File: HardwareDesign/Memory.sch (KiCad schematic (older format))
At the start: 4 parts, among them U200 28C256, U201 HM62256BLP-7SL

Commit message: more work on preparing for PCB design
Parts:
- added J201: Conn_02x40_Counter_Clockwise, symbol Connector_Generic:Conn_02x40_Counter_Clockwise
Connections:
- net labels added: E, PC0, PC1, PC2, PC3, PC4, PC5, PC6, PC7, RST, R~W, TIRQ, ~IODEV0, ~IODEV1, ~IODEV10, ~IODEV11, ~IODEV12, ~IODEV13, ~IODEV14, ~IODEV15, ~IODEV2, ~IODEV3, ~IODEV4, ~IODEV5, ~IODEV6, ~IODEV7, ~IODEV8, ~IODEV9, ~IRQ, ~RST~
- wire segments 95 -> 179
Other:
- note added: "back row"
- note added: "backplane connector"
- note added: "front row"
- moved on the sheet: C200, C201, U201

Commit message: more cleanups in preparation for PCB layout
Renamed nets to distinguish unbuffered vs. buffered signals.

Fixed one error in interrupt controller (D0 was tied
to ground.)

Not entirely done yet.
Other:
- note added: "back row (backplane)\nbottom row (board)"
- note added: "front row (backplane)\ntop row (board)"
- note removed: "back row"
- note removed: "front row"
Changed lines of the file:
@@
 Wire Wire Line
 	9050 5600 9600 5600
-Text Notes 8000 1450 0    50   ~ 0
-back row
-Text Notes 9300 1450 0    50   ~ 0
-front row
 Text Label 9400 1800 0    50   ~ 0
 D0
@@
 Wire Wire Line
 	7750 5950 7750 5850
+$Comp
+L power:VCC #PWR?
+U 1 1 60AC3A0A
+P 7750 5850
+F 0 "#PWR?" H 7750 5700 50  0001 C CNN
+F 1 "VCC" H 7767 6023 50  0000 C CNN
+F 2 "" H 7750 5850 50  0001 C CNN
+F 3 "" H 7750 5850 50  0001 C CNN
+	1    7750 5850
+	1    0    0    -1
+$EndComp
+Text Notes 7850 1500 0    50   ~ 0
+back row (backplane)\nbottom row (board)
+Text Notes 9000 1500 0    50   ~ 0
+front row (backplane)\ntop row (board)
 Wire Bus Line
 	3400 2950 6450 2950
@@
 Wire Bus Line
 	1500 1300 1500 3050
-$Comp
-L power:VCC #PWR?
-U 1 1 60AC3A0A
-P 7750 5850
-F 0 "#PWR?" H 7750 5700 50  0001 C CNN
-F 1 "VCC" H 7767 6023 50  0000 C CNN
-F 2 "" H 7750 5850 50  0001 C CNN
-F 3 "" H 7750 5850 50  0001 C CNN
-	1    7750 5850
-	1    0    0    -1
-$EndComp
 $EndSCHEMATC

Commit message: more preparations for PCB layout
More nets connected to appropriate backplane connector pin.
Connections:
- net labels added: ~IOR1~, ~IOR2~, ~IOR3~, ~IOR4~, ~IOR5~, ~IOR6~, ~IOR7~
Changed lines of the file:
@@
 Text Notes 9000 1500 0    50   ~ 0
 front row (backplane)\ntop row (board)
+Text Label 8100 3300 0    50   ~ 0
+~IOR1~
+Text Label 8100 3400 0    50   ~ 0
+~IOR2~
+Text Label 8100 3500 0    50   ~ 0
+~IOR3~
+Text Label 8100 3600 0    50   ~ 0
+~IOR4~
+Text Label 8100 3700 0    50   ~ 0
+~IOR5~
+Text Label 8100 3800 0    50   ~ 0
+~IOR6~
+Text Label 8100 3900 0    50   ~ 0
+~IOR7~
 Wire Bus Line
 	3400 2950 6450 2950

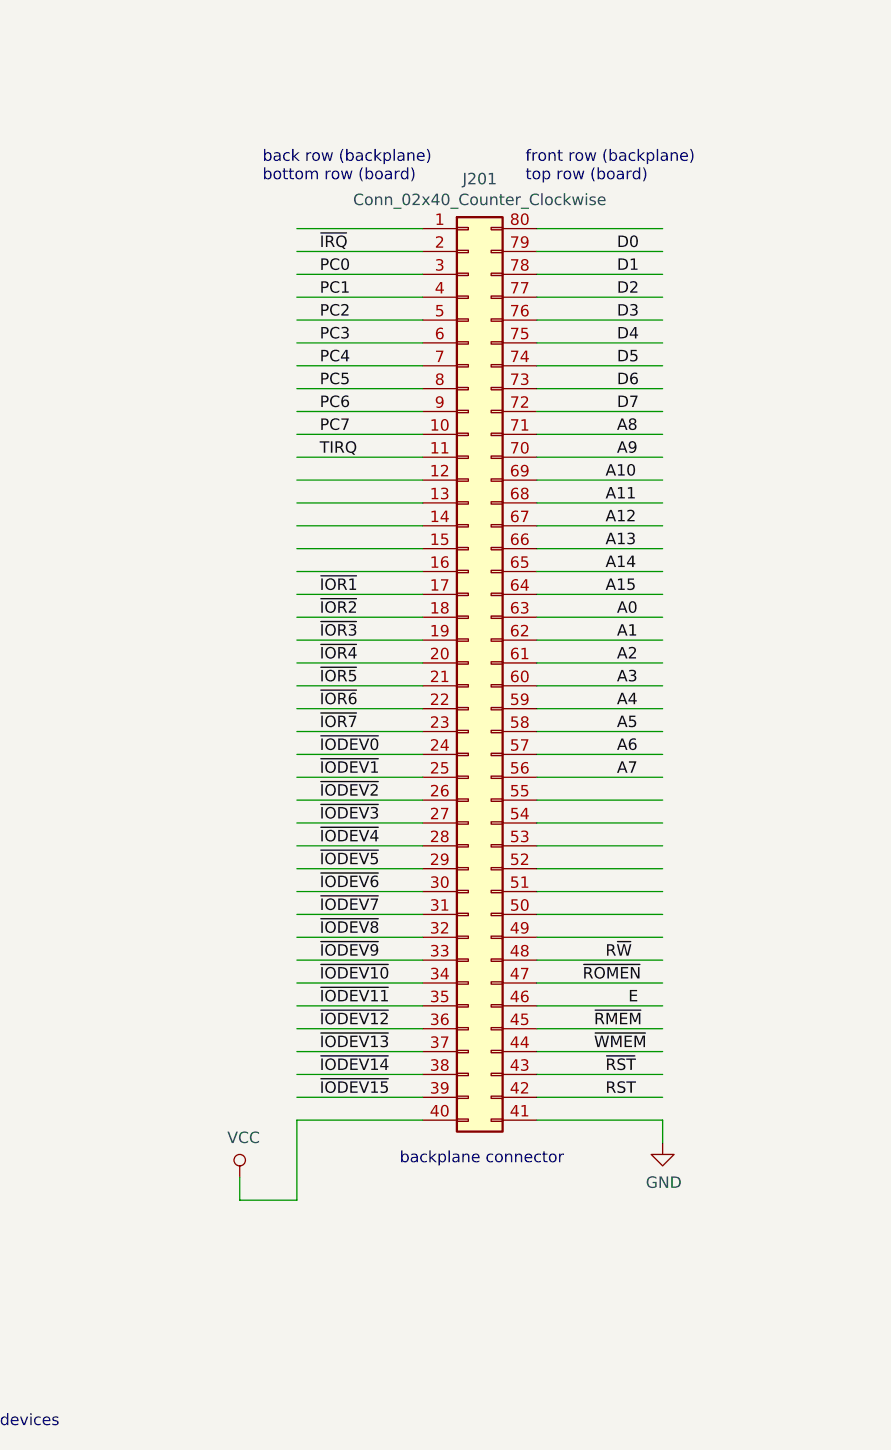
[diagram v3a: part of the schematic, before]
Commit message: more preparations for PCB layout
Make sure all nets connected to backplane connector pins are
labeled correctly.

Add bulk decoupling caps for each backplane connector.

Make keyboard interrupt be -IRQ5 rather than -IRQ7.
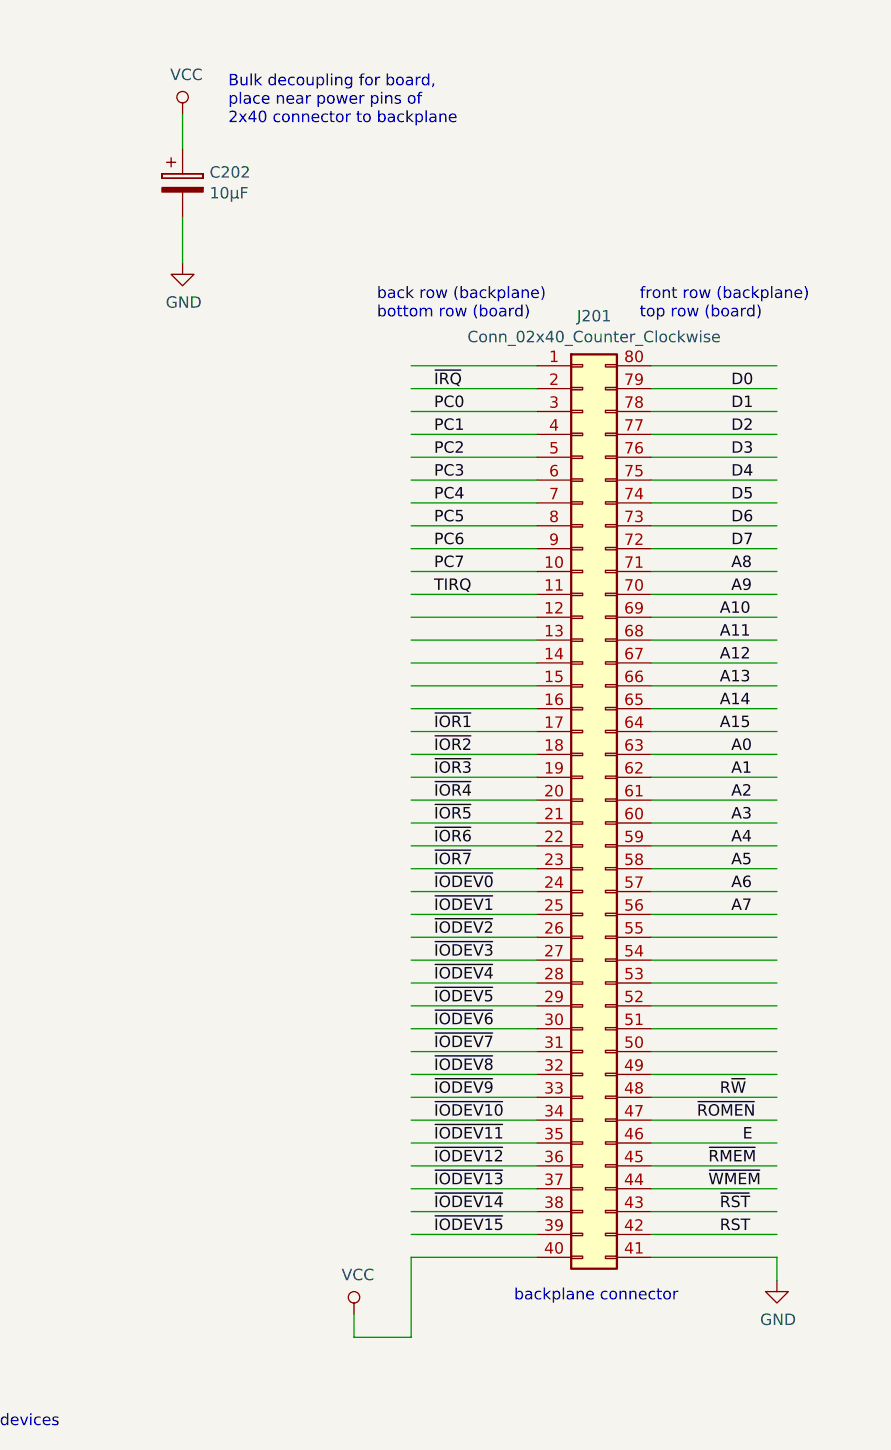
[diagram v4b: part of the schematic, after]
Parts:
- added C202: 10μF, symbol device:CP
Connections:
- wire segments 179 -> 181
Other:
- note added: "Bulk decoupling for board,\nplace near power pins of\n2x40 connector to backplane"
- moved on the sheet: J201

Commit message: a few more consistency tweaks before PCB layout
Routed second timer/counter output to backplane connector,
just in case we want to use it for something eventually
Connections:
- net labels added: TCOUNT2
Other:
- note added: "TCOUNT2 shown here\nto allow second\ntimer/counter output\nto connect to backplane"
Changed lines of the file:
@@
 U 1 1 60CC0A73
 P 7500 1200
+AR Path="/5CFA6AAA/60CC0A73" Ref="#PWR?"  Part="1"
+AR Path="/5D49B078/60CC0A73" Ref="#PWR?"  Part="1"
 F 0 "#PWR?" H 7500 1050 50  0001 C CNN
 F 1 "VCC" H 7517 1373 50  0000 C CNN
@@
 U 1 1 60CC0A7A
 P 7500 1850
+AR Path="/5CFA6AAA/60CC0A7A" Ref="#PWR?"  Part="1"
+AR Path="/5D49B078/60CC0A7A" Ref="#PWR?"  Part="1"
 F 0 "#PWR?" H 7500 1600 50  0001 C CNN
 F 1 "GND" H 7505 1677 50  0000 C CNN
@@
 Wire Bus Line
 	1500 1300 1500 3050
+Text Label 8600 3400 0    50   ~ 0
+TCOUNT2
+Text HLabel 8500 3400 0    50   Input ~ 0
+TCOUNT2
+Text Notes 7450 3300 0    50   ~ 0
+TCOUNT2 shown here\nto allow second\ntimer/counter output\nto connect to backplane
 $EndSCHEMATC

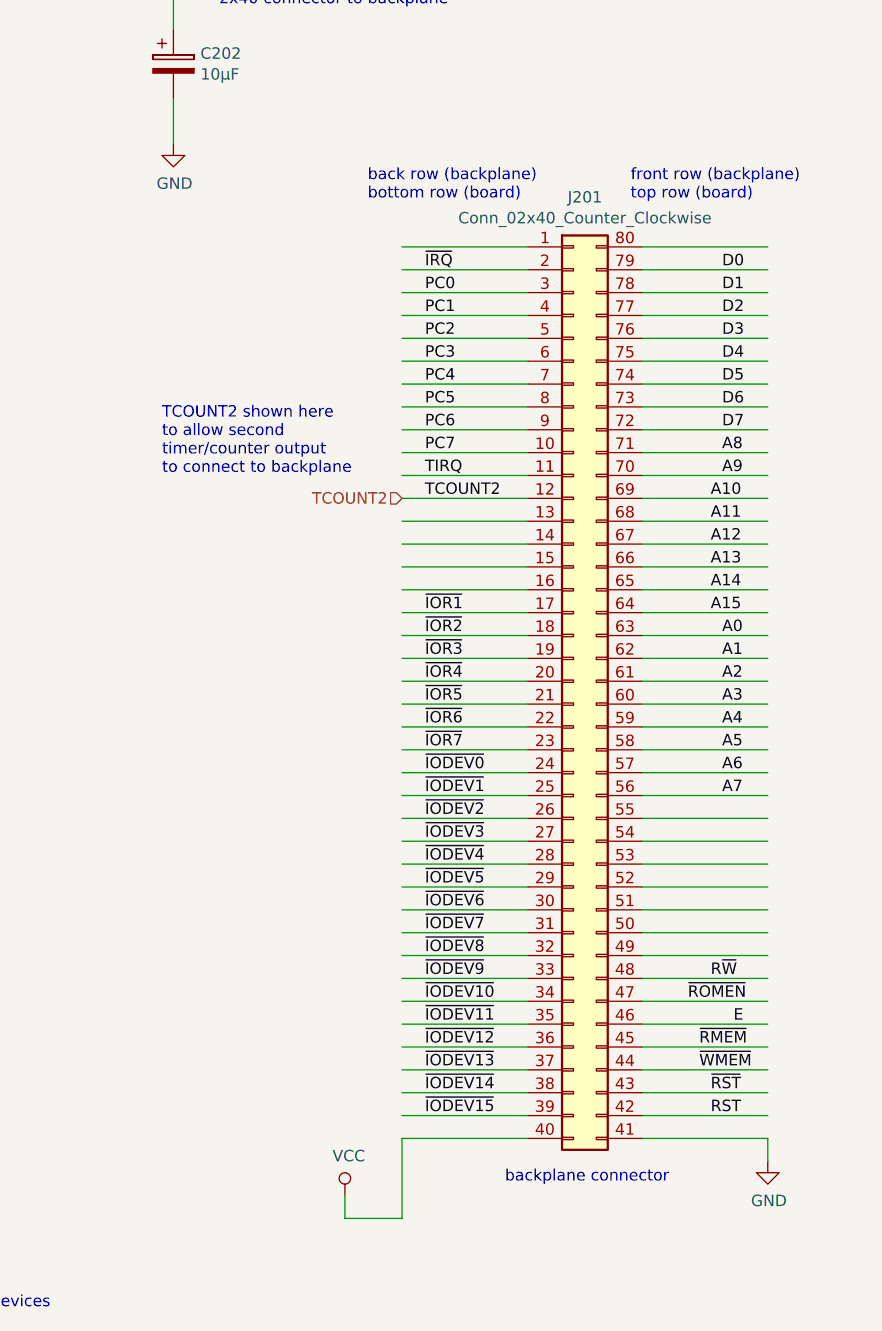
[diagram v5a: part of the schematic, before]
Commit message: have one copy of backplane connector on main sheet
Avoids need to replicate it elsewhere, and helps ensure
that all signals are connected correctly.
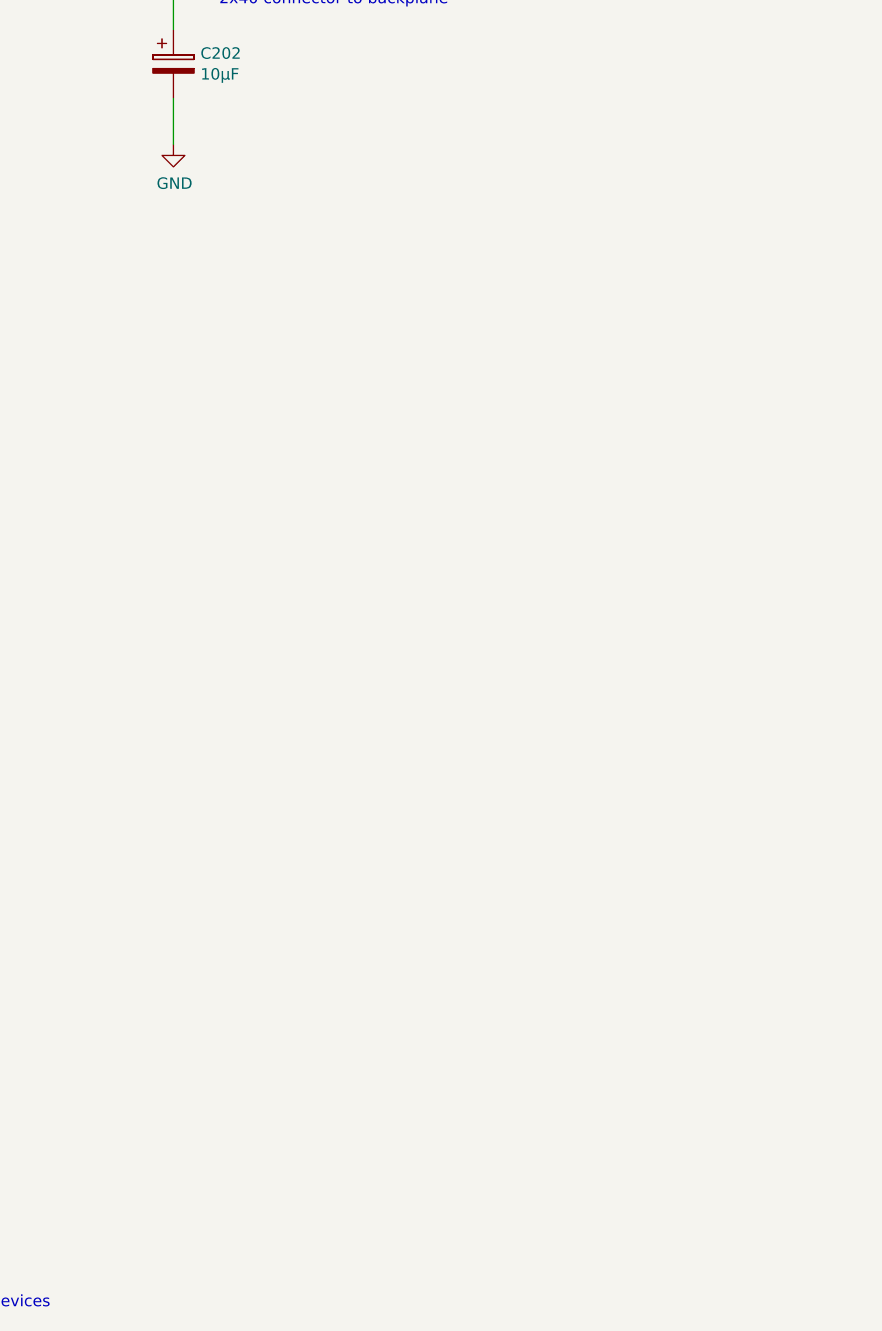
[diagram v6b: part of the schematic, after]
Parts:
- removed J201: Conn_02x40_Counter_Clockwise, symbol Connector_Generic:Conn_02x40_Counter_Clockwise
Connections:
- net labels removed: E, PC0, PC1, PC2, PC3, PC4, PC5, PC6, PC7, RST, R~W, TCOUNT2, TIRQ, ~IODEV0, ~IODEV1, ~IODEV10, ~IODEV11, ~IODEV12, ~IODEV13, ~IODEV14, ~IODEV15, ~IODEV2, ~IODEV3, ~IODEV4, ~IODEV5, ~IODEV6, ~IODEV7, ~IODEV8, ~IODEV9, ~IOR1~, ~IOR2~, ~IOR3~, ~IOR4~, ~IOR5~, ~IOR6~, ~IOR7~, ~IRQ, ~RST~
- wire segments 181 -> 97
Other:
- note removed: "TCOUNT2 shown here\nto allow second\ntimer/counter output\nto connect to backplane"
- note removed: "back row (backplane)\nbottom row (board)"
- note removed: "backplane connector"
- note removed: "front row (backplane)\ntop row (board)"

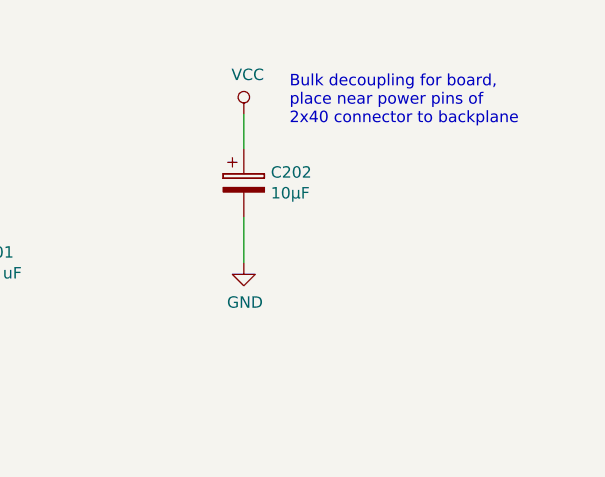
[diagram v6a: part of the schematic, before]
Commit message: assigned component footprints
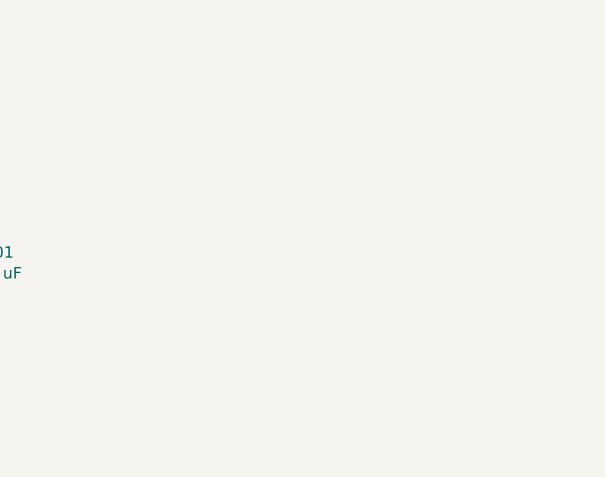
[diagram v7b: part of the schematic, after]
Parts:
- removed C202: 10μF, symbol device:CP
- C200, C201: footprint (none) -> Capacitor_THT:C_Disc_D5.0mm_W2.5mm_P2.50mm
- U200: footprint (none) -> Socket:DIP_Socket-28_W11.9_W12.7_W15.24_W17.78_W18.5_3M_228-1277-00-0602J
- U201: footprint DIP28 -> Package_DIP:DIP-28_W15.24mm_Socket
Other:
- note removed: "Bulk decoupling for board,\nplace near power pins of\n2x40 connector to backplane"
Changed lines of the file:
@@
 F 0 "U200" H 3150 5678 50  0000 C CNN
 F 1 "28C256" H 3150 5587 50  0000 C CNN
-F 2 "" H 3150 4500 50  0001 C CNN
+F 2 "Socket:DIP_Socket-28_W11.9_W12.7_W15.24_W17.78_W18.5_3M_228-1277-00-0602J" H 3150 4500 50  0001 C CNN
 F 3 "" H 3150 4500 50  0001 C CNN
 	1    3150 4500
@@
 F 0 "U201" H 5600 5528 50  0000 C CNN
 F 1 "HM62256BLP-7SL" H 5600 5437 50  0000 C CNN
-F 2 "DIP28" H 5600 4450 50  0001 C CIN
+F 2 "Package_DIP:DIP-28_W15.24mm_Socket" H 5600 4450 50  0001 C CIN
 F 3 "" H 5600 4450 50  0001 C CNN
 	1    5600 4450
@@
 F 0 "C200" H 5715 1896 50  0000 L CNN
 F 1 "0.1 uF" H 5715 1805 50  0000 L CNN
-F 2 "" H 5638 1700 50  0001 C CNN
+F 2 "Capacitor_THT:C_Disc_D5.0mm_W2.5mm_P2.50mm" H 5638 1700 50  0001 C CNN
 F 3 "" H 5600 1850 50  0001 C CNN
 	1    5600 1850
@@
 F 0 "C201" H 6315 1896 50  0000 L CNN
 F 1 "0.1 uF" H 6315 1805 50  0000 L CNN
-F 2 "" H 6238 1700 50  0001 C CNN
+F 2 "Capacitor_THT:C_Disc_D5.0mm_W2.5mm_P2.50mm" H 6238 1700 50  0001 C CNN
 F 3 "" H 6200 1850 50  0001 C CNN
 	1    6200 1850
@@
 Text Label 4900 5400 0    50   ~ 0
 A15
-$Comp
-L device:CP C?
-U 1 1 60CC0A6C
-P 7500 1500
-AR Path="/5CFA6AAA/60CC0A6C" Ref="C?"  Part="1"
-AR Path="/5D49B078/60CC0A6C" Ref="C202"  Part="1"
-F 0 "C202" H 7618 1546 50  0000 L CNN
-F 1 "10μF" H 7618 1455 50  0000 L CNN
-F 2 "" H 7538 1350 50  0001 C CNN
-F 3 "" H 7500 1500 50  0001 C CNN
-	1    7500 1500
-	1    0    0    -1
-$EndComp
-Wire Wire Line
-	7500 1350 7500 1200
-$Comp
-L power:VCC #PWR?
-U 1 1 60CC0A73
-P 7500 1200
-AR Path="/5CFA6AAA/60CC0A73" Ref="#PWR?"  Part="1"
-AR Path="/5D49B078/60CC0A73" Ref="#PWR?"  Part="1"
-F 0 "#PWR?" H 7500 1050 50  0001 C CNN
-F 1 "VCC" H 7517 1373 50  0000 C CNN
-F 2 "" H 7500 1200 50  0001 C CNN
-F 3 "" H 7500 1200 50  0001 C CNN
-	1    7500 1200
-	1    0    0    -1
-$EndComp
-Wire Wire Line
-	7500 1650 7500 1850
-$Comp
-L power:GND #PWR?
-U 1 1 60CC0A7A
-P 7500 1850
-AR Path="/5CFA6AAA/60CC0A7A" Ref="#PWR?"  Part="1"
-AR Path="/5D49B078/60CC0A7A" Ref="#PWR?"  Part="1"
-F 0 "#PWR?" H 7500 1600 50  0001 C CNN
-F 1 "GND" H 7505 1677 50  0000 C CNN
-F 2 "" H 7500 1850 50  0001 C CNN
-F 3 "" H 7500 1850 50  0001 C CNN
-	1    7500 1850
-	1    0    0    -1
-$EndComp
-Text Notes 7700 1250 0    50   ~ 0
-Bulk decoupling for board,\nplace near power pins of\n2x40 connector to backplane
 Wire Bus Line
 	3400 2950 6450 2950
